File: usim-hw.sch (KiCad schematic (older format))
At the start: 32 parts, among them J2 Conn_01x06, SW1 SW_SPST, U1 MC6809, U2 MC6850, U3 62256, U4 28C256, U5 NE555P, U6 74LS10, U7 74LS04, Y1 2.4576M

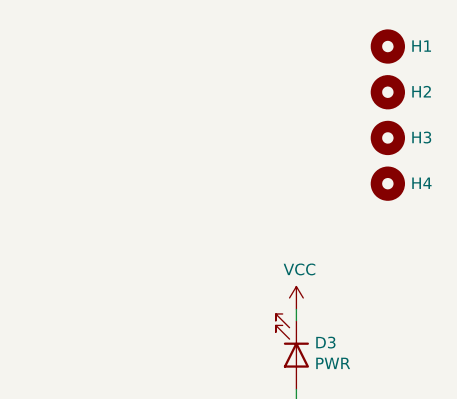
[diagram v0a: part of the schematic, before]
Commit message: switched to ZIF for EEPROM, shrunk by removing mt. holes
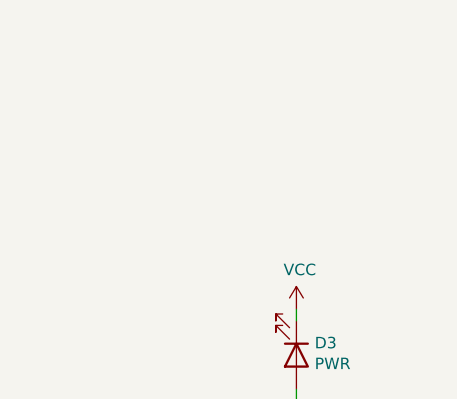
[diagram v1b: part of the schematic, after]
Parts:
- removed H1, H2, H3, H4: MountingHole, MountingHole:MountingHole_2.7mm_M2.5, symbol Mechanical:MountingHole
- U4: footprint Package_DIP:DIP-28_W15.24mm_Socket_LongPads -> Socket:DIP_Socket-28_W11.9_W12.7_W15.24_W17.78_W18.5_3M_228-1277-00-0602J
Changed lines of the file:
@@
 F 0 "U4" H 7250 2100 50  0000 C CNN
 F 1 "28C256" H 7300 2000 50  0000 C CNN
-F 2 "Package_DIP:DIP-28_W15.24mm_Socket_LongPads" H 7250 2000 50  0001 C CNN
+F 2 "Socket:DIP_Socket-28_W11.9_W12.7_W15.24_W17.78_W18.5_3M_228-1277-00-0602J" H 7250 2000 50  0001 C CNN
 F 3 "http://ww1.microchip.com/downloads/en/DeviceDoc/doc0006.pdf" H 7250 2000 50  0001 C CNN
 	1    7250 2000
@@
 Wire Wire Line
 	3650 5100 3650 5050
-$Comp
-L Mechanical:MountingHole H1
-U 1 1 6470C51B
-P 10250 650
-F 0 "H1" H 10350 650 50  0000 L CNN
-F 1 "MountingHole" H 10350 605 50  0001 L CNN
-F 2 "MountingHole:MountingHole_2.7mm_M2.5" H 10250 650 50  0001 C CNN
-F 3 "~" H 10250 650 50  0001 C CNN
-	1    10250 650
-	1    0    0    -1
-$EndComp
-$Comp
-L Mechanical:MountingHole H2
-U 1 1 6470CC81
-P 10250 850
-F 0 "H2" H 10350 850 50  0000 L CNN
-F 1 "MountingHole" H 10350 805 50  0001 L CNN
-F 2 "MountingHole:MountingHole_2.7mm_M2.5" H 10250 850 50  0001 C CNN
-F 3 "~" H 10250 850 50  0001 C CNN
-	1    10250 850
-	1    0    0    -1
-$EndComp
-$Comp
-L Mechanical:MountingHole H3
-U 1 1 6470D177
-P 10250 1050
-F 0 "H3" H 10350 1050 50  0000 L CNN
-F 1 "MountingHole" H 10350 1005 50  0001 L CNN
-F 2 "MountingHole:MountingHole_2.7mm_M2.5" H 10250 1050 50  0001 C CNN
-F 3 "~" H 10250 1050 50  0001 C CNN
-	1    10250 1050
-	1    0    0    -1
-$EndComp
-$Comp
-L Mechanical:MountingHole H4
-U 1 1 6470D58F
-P 10250 1250
-F 0 "H4" H 10350 1250 50  0000 L CNN
-F 1 "MountingHole" H 10350 1205 50  0001 L CNN
-F 2 "MountingHole:MountingHole_2.7mm_M2.5" H 10250 1250 50  0001 C CNN
-F 3 "~" H 10250 1250 50  0001 C CNN
-	1    10250 1250
-	1    0    0    -1
-$EndComp
 Wire Wire Line
 	5400 1100 5650 1100

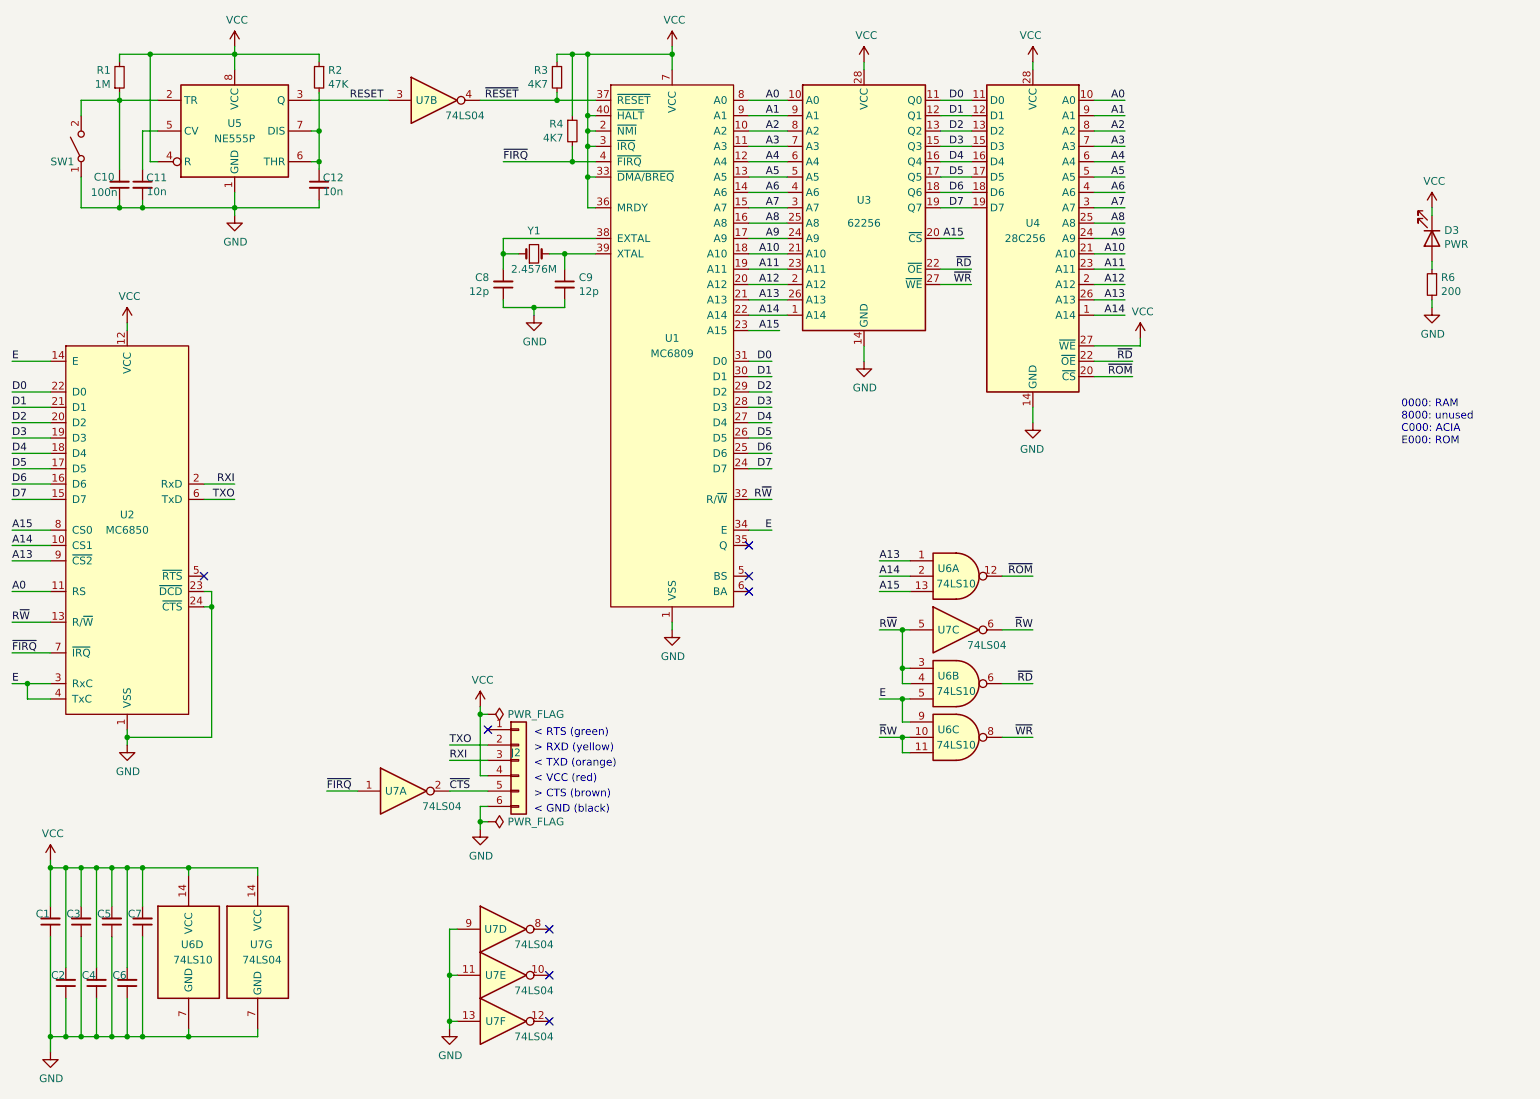
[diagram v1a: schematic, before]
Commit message: removed memory to shrink design; use separate memory board
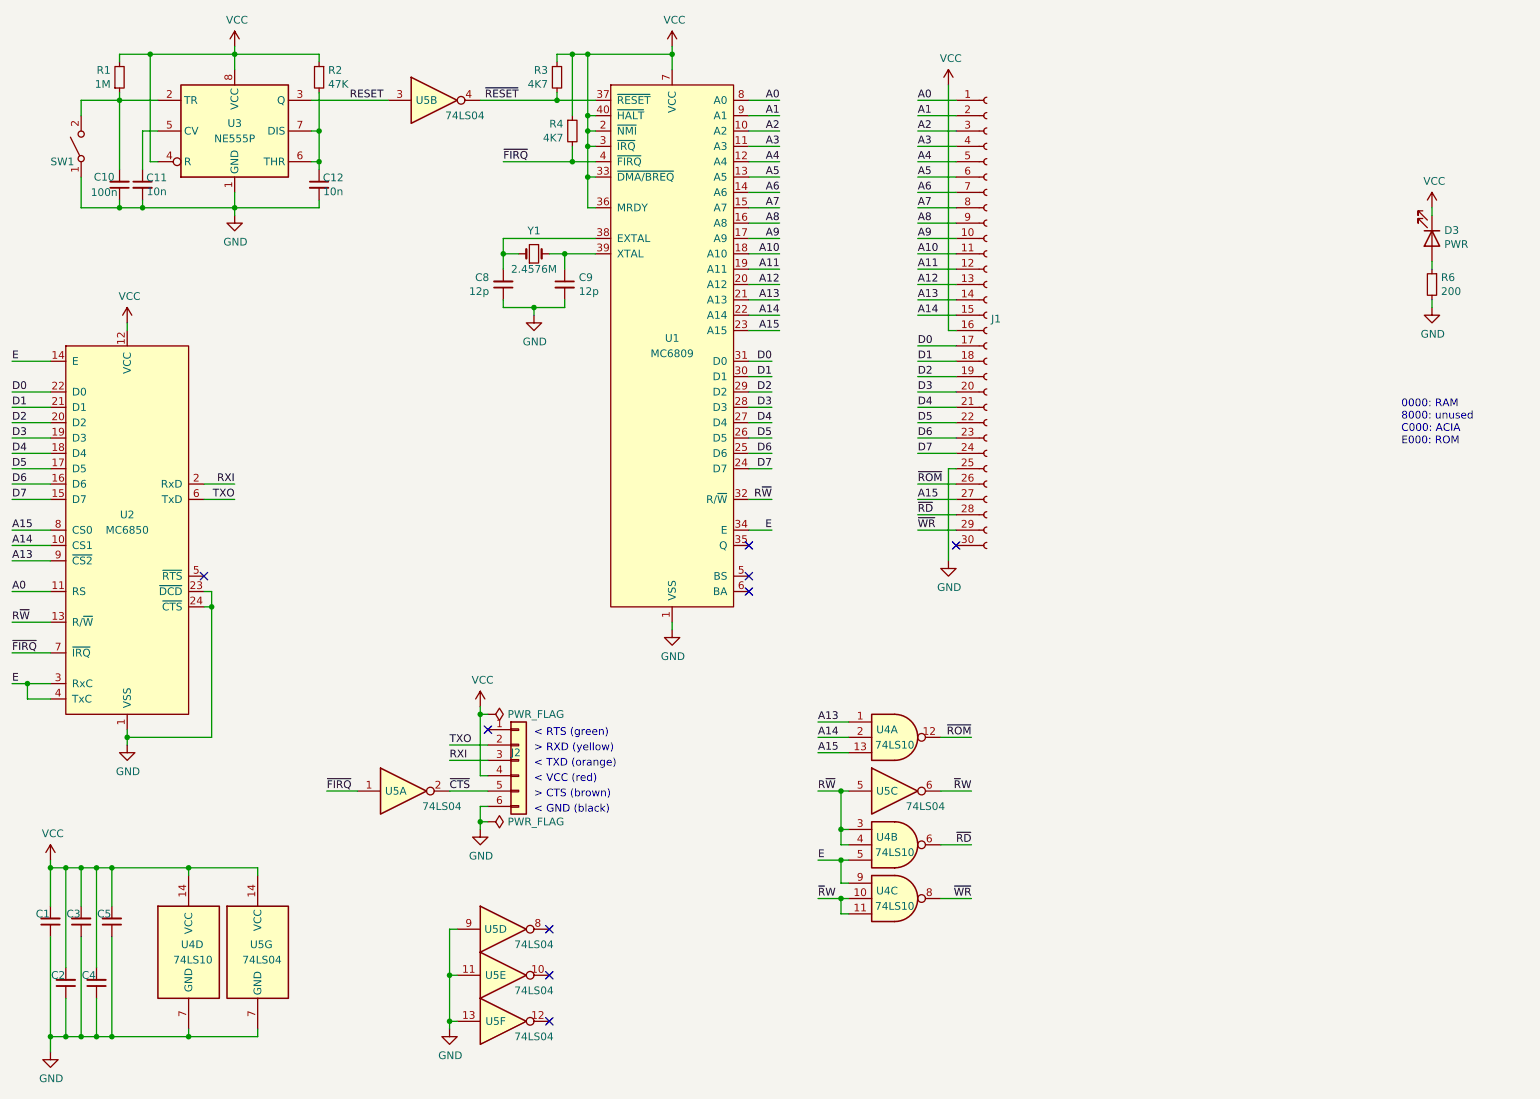
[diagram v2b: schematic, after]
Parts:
- removed C6, C7: 100n, Capacitor_THT:C_Disc_D3.0mm_W1.6mm_P2.50mm, symbol Device:C_Small
- removed U3: 62256, Package_DIP:DIP-28_W15.24mm_Socket_LongPads, symbol Memory_RAM:CY62256-70PC
- removed U4: 28C256, Socket:DIP_Socket-28_W11.9_W12.7_W15.24_W17.78_W18.5_3M_228-1277-00-0602J, symbol Memory_EEPROM:28C256
- added J1: Conn_01x30_Female, Connector_PinSocket_2.54mm:PinSocket_1x30_P2.54mm_Vertical, symbol Connector:Conn_01x30_Female
- renumbered U5 to U3, U6 to U4, U7 to U5
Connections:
- net A0: now also J1.1 (Pin_1)
- net A1: now also J1.2 (Pin_2)
- net A10: now also J1.11 (Pin_11)
- net A11: now also J1.12 (Pin_12)
- net A12: now also J1.13 (Pin_13)
- net A13: now also J1.14 (Pin_14)
- net A14: now also J1.15 (Pin_15)
- net A15: now also J1.27 (Pin_27)
- net A2: now also J1.3 (Pin_3)
- net A3: now also J1.4 (Pin_4)
- net A4: now also J1.5 (Pin_5)
- net A5: now also J1.6 (Pin_6)
- net A6: now also J1.7 (Pin_7)
- net A7: now also J1.8 (Pin_8)
- net A8: now also J1.9 (Pin_9)
- net A9: now also J1.10 (Pin_10)
- net D0: now also J1.17 (Pin_17)
- net D1: now also J1.18 (Pin_18)
- net D2: now also J1.19 (Pin_19)
- net D3: now also J1.20 (Pin_20)
- net D4: now also J1.21 (Pin_21)
- net D5: now also J1.22 (Pin_22)
- net D6: now also J1.23 (Pin_23)
- net D7: now also J1.24 (Pin_24)
- net GND: now also J1.25 (Pin_25)
- net VCC: now also J1.16 (Pin_16)
- net ~RD: now also J1.28 (Pin_28)
- net ~ROM: now also J1.26 (Pin_26)
- net ~WR: now also J1.29 (Pin_29)
- no-connect marks 8 -> 9
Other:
- moved on the sheet: U4A, U4B, U4C, U5C
